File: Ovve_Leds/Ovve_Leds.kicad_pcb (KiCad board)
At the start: 2 copper layers, 116 parts, among them J1 Conn_01x04, J2 Conn_01x04, J3 Conn_01x04, J4 Conn_01x04, J5 Conn_01x04, J6 Conn_01x04, J7 Conn_01x04, J8 Conn_01x02, U1 74LS174, U2 74LS174, U3 74LS174, U4 74LS174

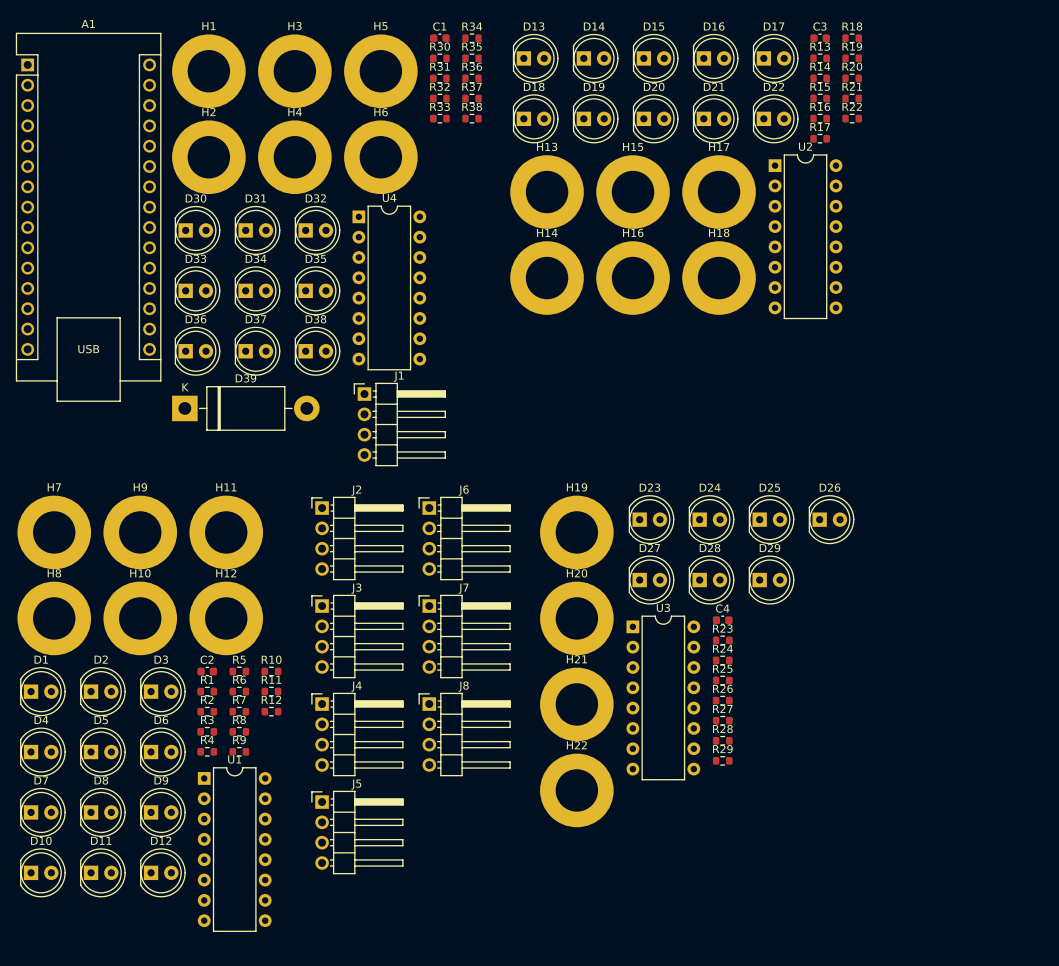
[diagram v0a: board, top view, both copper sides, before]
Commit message: updated footprint of connector
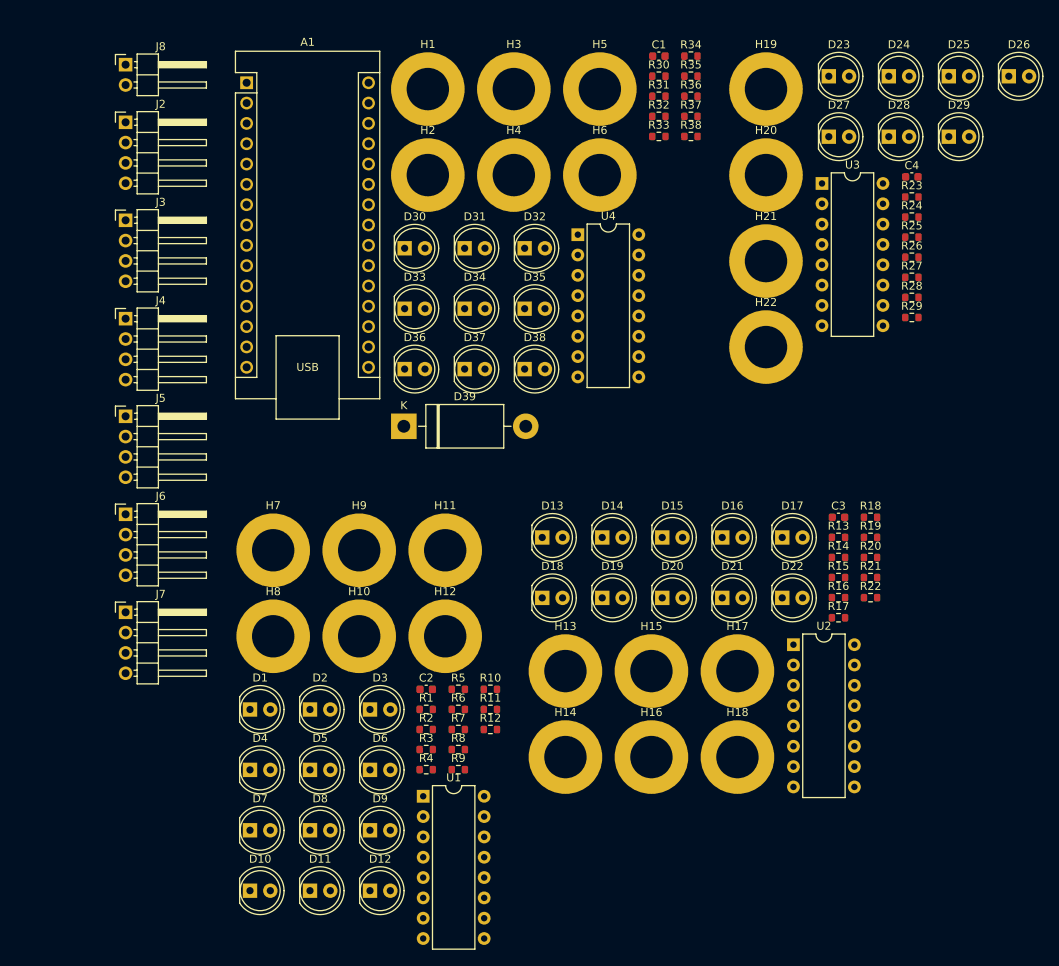
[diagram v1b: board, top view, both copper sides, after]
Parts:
- removed J1: Conn_01x04, Connector_PinHeader_2.54mm:PinHeader_1x04_P2.54mm_Horizontal
- J8: footprint Connector_PinHeader_2.54mm:PinHeader_1x04_P2.54mm_Horizontal -> Connector_PinHeader_2.54mm:PinHeader_1x02_P2.54mm_Horizontal
- moved J8 88.5 mm to (69.0, 64.0)
- moved C4 60.3 mm to (167.2, 78.0)
- moved D23 60.3 mm to (156.9, 65.4)
- moved D24 60.3 mm to (164.4, 65.4)
- moved D25 60.3 mm to (171.9, 65.4)
- moved D26 60.3 mm to (179.4, 65.4)
- moved D27 60.3 mm to (156.9, 73.0)
- moved D28 60.3 mm to (164.4, 73.0)
- moved D29 60.3 mm to (171.9, 73.0)
- moved H19 60.3 mm to (149.0, 67.0)
- moved H20 60.3 mm to (149.0, 77.8)
- moved H21 60.3 mm to (149.0, 88.5)
- moved H22 60.3 mm to (149.0, 99.2)
- moved R23 60.3 mm to (167.2, 80.5)
- moved R25 60.3 mm to (167.2, 85.5)
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
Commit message: Component layout on PCB
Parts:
- removed the H10 at (98.2, 135.4)
- removed the H15 at (134.7, 139.8)
- removed the H16 at (134.7, 150.5)
- removed the H21 at (149.0, 88.5)
- removed the H22 at (149.0, 99.2)
- removed H4, H5, H6: MountingHole, MountingHole:MountingHole_5.3mm_M5_DIN965_Pad
- removed the H9 at (98.2, 124.7)
- added H25: MountingHole, MountingHole:MountingHole_5.3mm_M5_DIN965_Pad, F.Cu at (405.0, 265.0)
- added H26: MountingHole, MountingHole:MountingHole_5.3mm_M5_DIN965_Pad, F.Cu at (485.0, 265.0)
- added H7: MountingHole, MountingHole:MountingHole_5.3mm_M5_DIN965_Pad, F.Cu at (105.0, 265.0)
- added H8: MountingHole, MountingHole:MountingHole_5.3mm_M5_DIN965_Pad, F.Cu at (185.0, 265.0)
- moved J7 391.0 mm to (456.2, 78.4), turned to 90 degrees
- moved D29 364.4 mm to (487.5, 255.0), turned to 180 degrees
- moved R29 351.1 mm to (480.0, 255.0)
- moved D28 336.6 mm to (447.5, 255.0), turned to 180 degrees
- moved H22 336.0 mm to (485.0, 82.0)
- moved J6 329.2 mm to (363.8, 266.6), turned to -90 degrees
- moved R28 327.8 mm to (455.0, 250.0), turned to 180 degrees
- moved D27 309.8 mm to (407.5, 255.0), turned to 180 degrees
- moved R27 294.8 mm to (415.2, 250.0), turned to 180 degrees
- moved J5 288.7 mm to (356.2, 78.4), turned to 90 degrees
- moved U3 286.5 mm to (442.5, 80.0), turned to -90 degrees
- moved C4 279.9 mm to (447.0, 87.3), turned to 90 degrees
- moved R26 276.3 mm to (415.2, 210.0), turned to 180 degrees
- moved D26 272.8 mm to (407.5, 215.0), turned to 180 degrees
- moved H16 269.9 mm to (385.0, 82.0)
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- renumbered H8 to H10, H11 to H13, H12 to H14, H13 to H15, H14 to H16, H17 to H19, H18 to H20, H19 to H21, H20 to H22, H7 to H9
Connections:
- net /Arduino_Power_A_letter/6V_in renamed /Arduino_Power_K_letter/6V_in
- net /Arduino_Power_A_letter/CLK renamed /Arduino_Power_K_letter/CLK
- net /Arduino_Power_A_letter/DATA renamed /Arduino_Power_K_letter/DATA
- net /Arduino_Power_A_letter/LED1 renamed /Arduino_Power_K_letter/LED1
- net /Arduino_Power_A_letter/LED2 renamed /Arduino_Power_K_letter/LED2
- net /Arduino_Power_A_letter/LED3 renamed /Arduino_Power_K_letter/LED3
- net /Arduino_Power_A_letter/LED4 renamed /Arduino_Power_K_letter/LED4
- net /Arduino_Power_A_letter/LED5 renamed /Arduino_Power_K_letter/LED5
- U1 pad 14: unconnected-(U1-D5-Pad14) -> GND
- U2 pad 14: unconnected-(U2-D5-Pad14) -> GND
- U3 pad 14: unconnected-(U3-D5-Pad14) -> GND
- U4 pad 14: unconnected-(U4-D5-Pad14) -> GND
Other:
- board outline added: 452 x 252 mm
- board text added: "4 AA battery holder"
- board text added: "Glue i guess?"

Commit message: Finished routing K and A
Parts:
- moved A1 3.62 mm to (148.9, 55.2)
- moved C1 3.62 mm to (165.2, 72.6)
- moved C2 3.62 mm to (247.0, 90.9)
- moved C3 3.62 mm to (347.0, 91.1)
- moved C4 3.62 mm to (447.0, 90.9)
- moved D1 3.62 mm to (207.5, 98.6)
- moved D10 3.62 mm to (287.5, 218.6)
- moved D11 3.62 mm to (207.5, 258.6)
- moved D12 3.62 mm to (287.5, 258.6)
- moved D13 3.62 mm to (307.5, 98.6)
- moved D14 3.62 mm to (347.5, 98.6)
- moved D15 3.62 mm to (307.5, 138.6)
- moved D16 3.62 mm to (387.5, 138.6)
- moved D17 3.62 mm to (307.5, 178.6)
- moved D18 3.62 mm to (347.5, 178.6)
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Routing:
- net +5V: track 0.00 -> 408.5 mm
- net /Arduino_Power_K_letter/CLK: track 0.00 -> 325.3 mm, vias 0 -> 2
- net /Arduino_Power_K_letter/LED5: track 0.00 -> 291.4 mm
- net /A_letter/CLK: track 0.00 -> 271.4 mm, vias 0 -> 2
- net /A_letter/LED5: track 0.00 -> 254.4 mm
- net /A_letter/LED4: track 0.00 -> 202.8 mm, vias 0 -> 2
- net /Arduino_Power_K_letter/LED4: track 0.00 -> 192.4 mm
- net /A_letter/LED3: track 0.00 -> 175.0 mm, vias 0 -> 2
- net /Arduino_Power_K_letter/LED3: track 0.00 -> 142.8 mm
- net /A_letter/LED2: track 0.00 -> 126.8 mm, vias 0 -> 2
- net /Arduino_Power_K_letter/LED1: track 0.00 -> 125.3 mm, vias 0 -> 2
- net /Arduino_Power_K_letter/LED2: track 0.00 -> 114.8 mm, vias 0 -> 2
- net /A_letter/LED1: track 0.00 -> 91.6 mm
- net /A_letter/DATA: track 0.00 -> 27.4 mm
- net /Arduino_Power_K_letter/DATA: track 0.00 -> 12.0 mm
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- added copper zone on B.Cu, net GND

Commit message: Finished routing
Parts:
- added G***: LOGO, Custom_Graphics:Alrakk_Rokaman_Correct, F.Cu at (72.0, 100.0)
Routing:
- net +5V: track 408.5 -> 1027.3 mm
- net /R_letter/LED5: track 0.00 -> 315.4 mm
- net /R_letter/CLK: track 0.00 -> 274.7 mm, vias 0 -> 2
- net /L_letter/LED5: track 0.00 -> 236.5 mm
- net /R_letter/LED4: track 0.00 -> 213.4 mm
- net /L_letter/LED4: track 0.00 -> 137.1 mm
- net /R_letter/LED3: track 0.00 -> 127.2 mm
- net /R_letter/LED2: track 0.00 -> 126.5 mm, vias 0 -> 2
- net /L_letter/LED3: track 0.00 -> 97.6 mm, vias 0 -> 2
- net /L_letter/LED2: track 0.00 -> 60.2 mm
- net /R_letter/LED1: track 0.00 -> 46.9 mm
- net /L_letter/CLK: track 0.00 -> 43.6 mm
- net /L_letter/LED1: track 0.00 -> 31.8 mm
- net /L_letter/DATA: track 0.00 -> 28.4 mm
- net /R_letter/DATA: track 0.00 -> 28.0 mm, vias 0 -> 2
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
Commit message: Started work on new design with only one letter
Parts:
- removed C1, C3, C4: 0.1u, Capacitor_SMD:C_0603_1608Metric
- removed D16, D17, D18, D19, D20, D21, D22, D23, D24, D25, D26, D27, D28, D29, D30, D31, D32, D33, D34, D35, D36, D37, D38: LED, LED_THT:LED_D5.0mm
- removed G***: LOGO, Custom_Graphics:Alrakk_Rokaman_Correct
- removed H10, H13, H14, H15, H16, H19, H20, H21, H22, H25, H26, H9: MountingHole, MountingHole:MountingHole_5.3mm_M5_DIN965_Pad
- removed J5, J6, J7: Conn_01x04, Connector_PinHeader_2.54mm:PinHeader_1x04_P2.54mm_Horizontal
- removed R16, R17, R18, R19, R20, R21, R22, R23, R24, R25, R26, R27, R28, R29, R30, R31, R32, R33, R34, R35, R36, R37, R38: 150, Resistor_SMD:R_0603_1608Metric
- removed U2, U3, U4: 74LS174, Package_DIP:DIP-16_W7.62mm
- added H4: MountingHole, MountingHole:MountingHole_5.3mm_M5_DIN965_Pad, F.Cu at (169.0, 140.0)
- added H5: MountingHole, MountingHole:MountingHole_5.3mm_M5_DIN965_Pad, F.Cu at (211.0, 161.0)
- added H6: MountingHole, MountingHole:MountingHole_5.3mm_M5_DIN965_Pad, F.Cu at (299.0, 161.0)
- moved D11 159.0 mm to (261.5, 109.1), turned to 0 degrees
- moved J2 157.7 mm to (178.6, 113.2), turned to 0 degrees
- moved R12 152.8 mm to (284.1, 105.8)
- moved D12 150.7 mm to (269.0, 109.1), turned to 0 degrees
- moved R11 150.0 mm to (280.0, 118.4), turned to 0 degrees
- moved H1 147.1 mm to (169.0, 107.7)
- moved D9 132.2 mm to (269.0, 101.5), turned to 0 degrees
- moved H3 125.7 mm to (169.0, 129.2)
- moved R9 119.4 mm to (280.0, 113.4), turned to 0 degrees
- moved H8 118.0 mm to (299.0, 299.0)
- moved D10 114.5 mm to (254.0, 109.1), turned to 0 degrees
- moved H7 110.3 mm to (211.0, 299.0)
- moved D6 104.6 mm to (269.0, 94.0), turned to 0 degrees
- moved R10 102.8 mm to (280.0, 115.9)
- moved J8 99.7 mm to (192.0, 113.2), turned to 0 degrees
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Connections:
- J2 pad 1: /Arduino_Power_K_letter/LED5 -> /Arduino_Power_K_letter/DATA
- J3 pad 1: GND -> /GND_in_A
- J3 pad 2: +5V -> /Vcc_in_A
- J3 pad 3: /A_letter/CLK -> /CLK_in_A
- J3 pad 4: /A_letter/DATA -> /DATA_in_A
- J4 pad 1: /A_letter/LED5 -> /DATA_out_A
- J4 pad 2: /A_letter/CLK -> /CLK_out_A
- J4 pad 3: +5V -> /Vcc_out_A
- J4 pad 4: GND -> /GND_out_A
- R11 pad 1: /A_letter/LED5 -> /A_letter/LED4
- R12 pad 1: /A_letter/LED5 -> /A_letter/LED4
- R13 pad 1: /R_letter/LED1 -> /A_letter/LED5
- R14 pad 1: /R_letter/LED1 -> /A_letter/LED5
- R15 pad 1: /R_letter/LED2 -> /A_letter/LED5
- R6 pad 1: /A_letter/LED3 -> /A_letter/LED2
- R9 pad 1: /A_letter/LED4 -> /A_letter/LED3
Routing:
- net +5V: track 1027.3 -> 0.00 mm
- net /Arduino_Power_K_letter/CLK: track 325.3 -> 0.00 mm, vias 2 -> 0
- net /R_letter/LED5: track 315.4 -> 0.00 mm
- net /Arduino_Power_K_letter/LED5: track 291.4 -> 0.00 mm
- net /R_letter/CLK: track 274.7 -> 0.00 mm, vias 2 -> 0
- net /A_letter/CLK: track 271.4 -> 0.00 mm, vias 2 -> 0
- net /A_letter/LED5: track 254.4 -> 0.00 mm
- net /L_letter/LED5: track 236.5 -> 0.00 mm
- net /R_letter/LED4: track 213.4 -> 0.00 mm
- net /A_letter/LED4: track 202.6 -> 0.00 mm, vias 2 -> 0
- net /Arduino_Power_K_letter/LED4: track 192.4 -> 0.00 mm
- net /A_letter/LED3: track 175.0 -> 0.00 mm, vias 2 -> 0
- net /Arduino_Power_K_letter/LED3: track 142.8 -> 0.00 mm
- net /L_letter/LED4: track 137.1 -> 0.00 mm
- net /R_letter/LED3: track 127.2 -> 0.00 mm
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- removed copper zone on B.Cu, net GND
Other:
- board size 452 x 252 mm -> 100 x 150 mm
- board text removed: "4 AA battery holder"
- board text removed: "Glue i guess?"

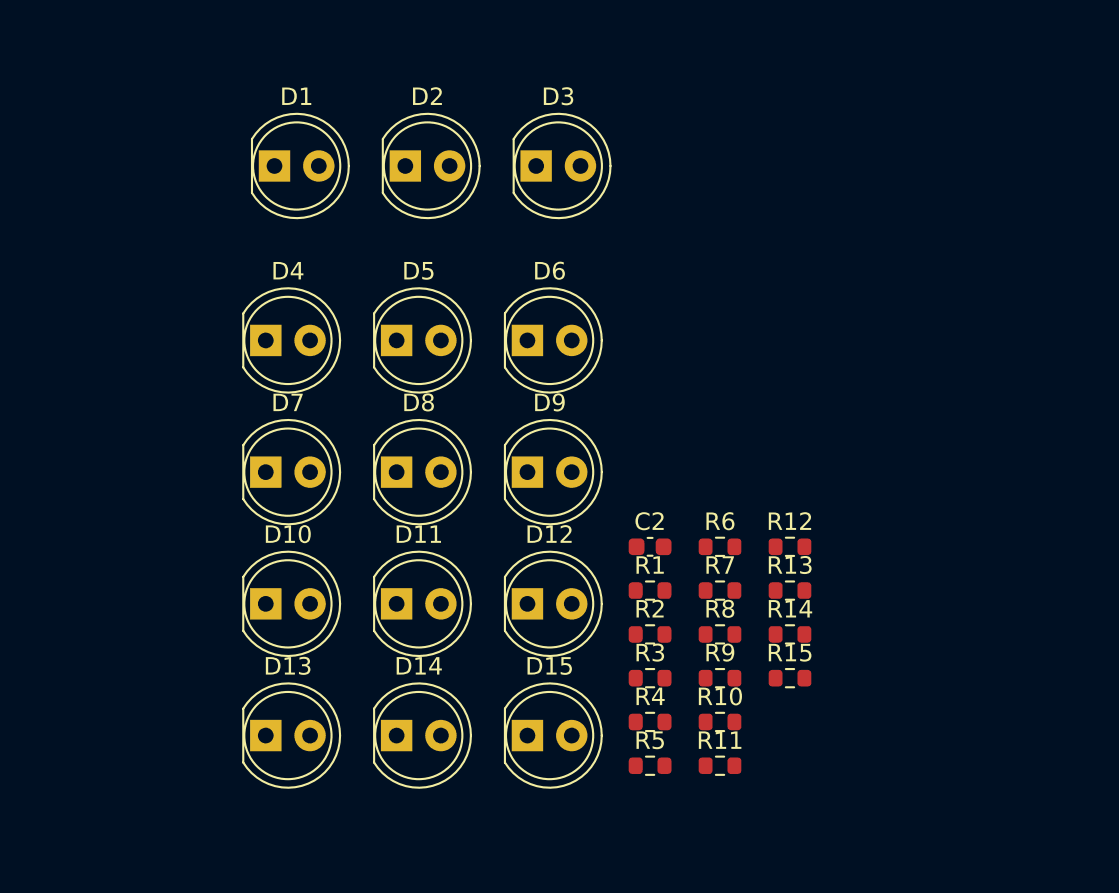
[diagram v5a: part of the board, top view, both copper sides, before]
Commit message: Added more LEDs to make letters more visible since there will be no silkscreen
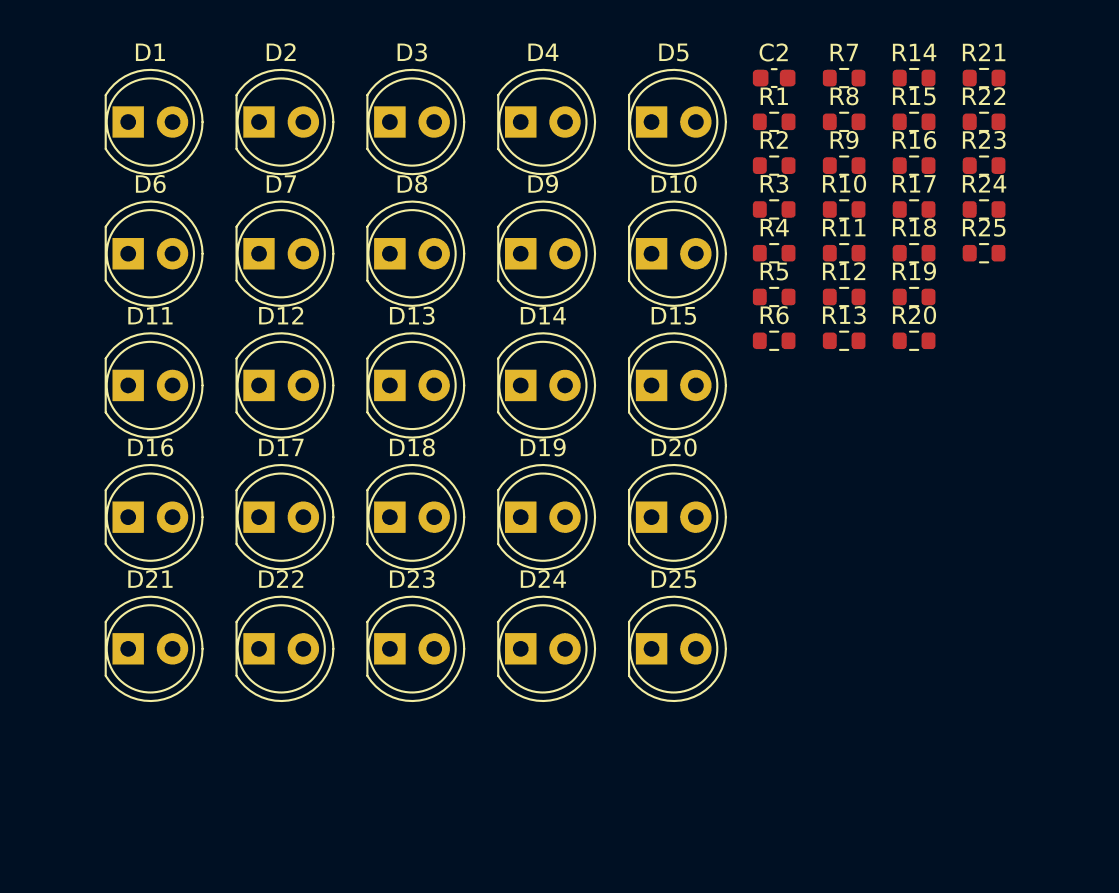
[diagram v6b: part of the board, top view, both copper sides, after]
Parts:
- added D16: LED, LED_THT:LED_D5.0mm, F.Cu at (246.1, 104.1)
- added D17: LED, LED_THT:LED_D5.0mm, F.Cu at (253.6, 104.1)
- added D18: LED, LED_THT:LED_D5.0mm, F.Cu at (261.1, 104.1)
- added D19: LED, LED_THT:LED_D5.0mm, F.Cu at (268.6, 104.1)
- added D20: LED, LED_THT:LED_D5.0mm, F.Cu at (276.1, 104.1)
- added D21: LED, LED_THT:LED_D5.0mm, F.Cu at (246.1, 111.7)
- added D22: LED, LED_THT:LED_D5.0mm, F.Cu at (253.6, 111.7)
- added D23: LED, LED_THT:LED_D5.0mm, F.Cu at (261.1, 111.7)
- added D24: LED, LED_THT:LED_D5.0mm, F.Cu at (268.6, 111.7)
- added D25: LED, LED_THT:LED_D5.0mm, F.Cu at (276.1, 111.7)
- added R16: 150, Resistor_SMD:R_0603_1608Metric, F.Cu at (291.2, 84.0)
- added R17: 150, Resistor_SMD:R_0603_1608Metric, F.Cu at (291.2, 86.5)
- added R18: 150, Resistor_SMD:R_0603_1608Metric, F.Cu at (291.2, 89.0)
- added R19: 150, Resistor_SMD:R_0603_1608Metric, F.Cu at (291.2, 91.5)
- added R20: 150, Resistor_SMD:R_0603_1608Metric, F.Cu at (291.2, 94.0)
- added R21: 150, Resistor_SMD:R_0603_1608Metric, F.Cu at (295.2, 79.0)
- added R22: 150, Resistor_SMD:R_0603_1608Metric, F.Cu at (295.2, 81.5)
- added R23: 150, Resistor_SMD:R_0603_1608Metric, F.Cu at (295.2, 84.0)
- added R24: 150, Resistor_SMD:R_0603_1608Metric, F.Cu at (295.2, 86.5)
- added R25: 150, Resistor_SMD:R_0603_1608Metric, F.Cu at (295.2, 89.0)
- moved R14 32.7 mm to (291.2, 79.0)
- moved R15 32.7 mm to (291.2, 81.5)
- moved R10 30.2 mm to (287.2, 86.5)
- moved R7 30.2 mm to (287.2, 79.0)
- moved R11 30.2 mm to (287.2, 89.0)
- moved R8 30.2 mm to (287.2, 81.5)
- moved R9 30.2 mm to (287.2, 84.0)
- moved D10 29.9 mm to (276.1, 89.0)
- moved C2 27.8 mm to (283.1, 79.0)
- moved R1 27.8 mm to (283.1, 81.5)
- moved R3 27.8 mm to (283.1, 86.5)
- moved R4 27.8 mm to (283.1, 89.0)
- moved R2 27.8 mm to (283.1, 84.0)
- moved R5 27.8 mm to (283.1, 91.5)
- moved D6 23.4 mm to (246.1, 89.0)
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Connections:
- R10 pad 1: /A_letter/LED4 -> /A_letter/LED2
- R11 pad 1: /A_letter/LED4 -> /A_letter/LED3
- R12 pad 1: /A_letter/LED4 -> /A_letter/LED3
- R13 pad 1: /A_letter/LED5 -> /A_letter/LED3
- R14 pad 1: /A_letter/LED5 -> /A_letter/LED3
- R15 pad 1: /A_letter/LED5 -> /A_letter/LED3
- R4 pad 1: /A_letter/LED2 -> /A_letter/LED1
- R5 pad 1: /A_letter/LED2 -> /A_letter/LED1
- R7 pad 1: /A_letter/LED3 -> /A_letter/LED2
- R8 pad 1: /A_letter/LED3 -> /A_letter/LED2
- R9 pad 1: /A_letter/LED3 -> /A_letter/LED2

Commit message: Changed to 5x4
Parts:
- removed D21, D22, D23, D24, D25: LED, LED_THT:LED_D5.0mm
- removed R21, R22, R23, R24, R25: 150, Resistor_SMD:R_0603_1608Metric
- moved D5 34.5 mm to (243.6, 93.0)
- moved D10 27.5 mm to (251.1, 100.6)
- moved D9 27.5 mm to (243.6, 100.6)
- moved D13 20.9 mm to (243.6, 108.1)
- moved D14 20.9 mm to (251.1, 108.1)
- moved D15 20.9 mm to (258.6, 108.1)
- moved D16 20.4 mm to (266.1, 108.1)
- moved D17 15.3 mm to (243.6, 115.7)
- moved D18 15.3 mm to (251.1, 115.7)
- moved D19 15.3 mm to (258.6, 115.7)
- moved D20 15.3 mm to (266.1, 115.7)
- moved D11 13.1 mm to (258.6, 100.6)
- moved D12 13.1 mm to (266.1, 100.6)
- moved C2 10.8 mm to (273.2, 82.9)
- moved R1 10.8 mm to (273.2, 85.5)
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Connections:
- R10 pad 1: /A_letter/LED2 -> /A_letter/LED3
- R13 pad 1: /A_letter/LED3 -> /A_letter/LED4
- R14 pad 1: /A_letter/LED3 -> /A_letter/LED4
- R15 pad 1: /A_letter/LED3 -> /A_letter/LED4
- R17 pad 1: /A_letter/LED4 -> /A_letter/LED5
- R18 pad 1: /A_letter/LED4 -> /A_letter/LED5
- R19 pad 1: /A_letter/LED4 -> /A_letter/LED5
- R20 pad 1: /A_letter/LED4 -> /A_letter/LED5
- R5 pad 1: /A_letter/LED1 -> /A_letter/LED2
- R9 pad 1: /A_letter/LED2 -> /A_letter/LED3

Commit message: problem with CLK not connecting
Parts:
- added J1: Conn_01x04, Connector_PinHeader_2.54mm:PinHeader_1x04_P2.54mm_Horizontal, F.Cu at (1.82, 1.82)
- moved R17 199.3 mm to (226.2, 282.0), turned to 180 degrees
- moved R18 192.3 mm to (246.0, 282.0), turned to 180 degrees
- moved R19 187.1 mm to (266.2, 282.0), turned to 180 degrees
- moved R20 184.1 mm to (286.2, 282.0), turned to 180 degrees
- moved R14 174.6 mm to (246.2, 254.0), turned to 180 degrees
- moved C2 174.4 mm to (254.0, 256.3)
- moved D20 173.9 mm to (285.0, 288.5), turned to 90 degrees
- moved D17 173.9 mm to (225.0, 288.5), turned to 90 degrees
- moved D19 173.0 mm to (265.0, 288.5), turned to 90 degrees
- moved D18 173.0 mm to (245.0, 288.5), turned to 90 degrees
- moved R15 169.2 mm to (266.2, 254.0), turned to 180 degrees
- moved R16 166.1 mm to (286.0, 254.0), turned to 180 degrees
- moved R13 164.2 mm to (226.0, 254.0), turned to 180 degrees
- moved D13 153.6 mm to (225.0, 260.5), turned to 90 degrees
- moved D16 153.6 mm to (285.0, 260.5), turned to 90 degrees
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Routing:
- added copper zone on B.Cu, net GND
